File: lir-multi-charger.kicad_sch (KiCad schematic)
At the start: 43 parts, among them J1 USB_C_Receptacle_USB2.0, J2 Conn_01x02_Male, J3 Conn_01x02_Male, J4 Conn_01x02_Male, J5 Conn_01x02_Male, J6 Conn_01x02_Male, U1 CN3130, U2 CN3130, U3 CN3130

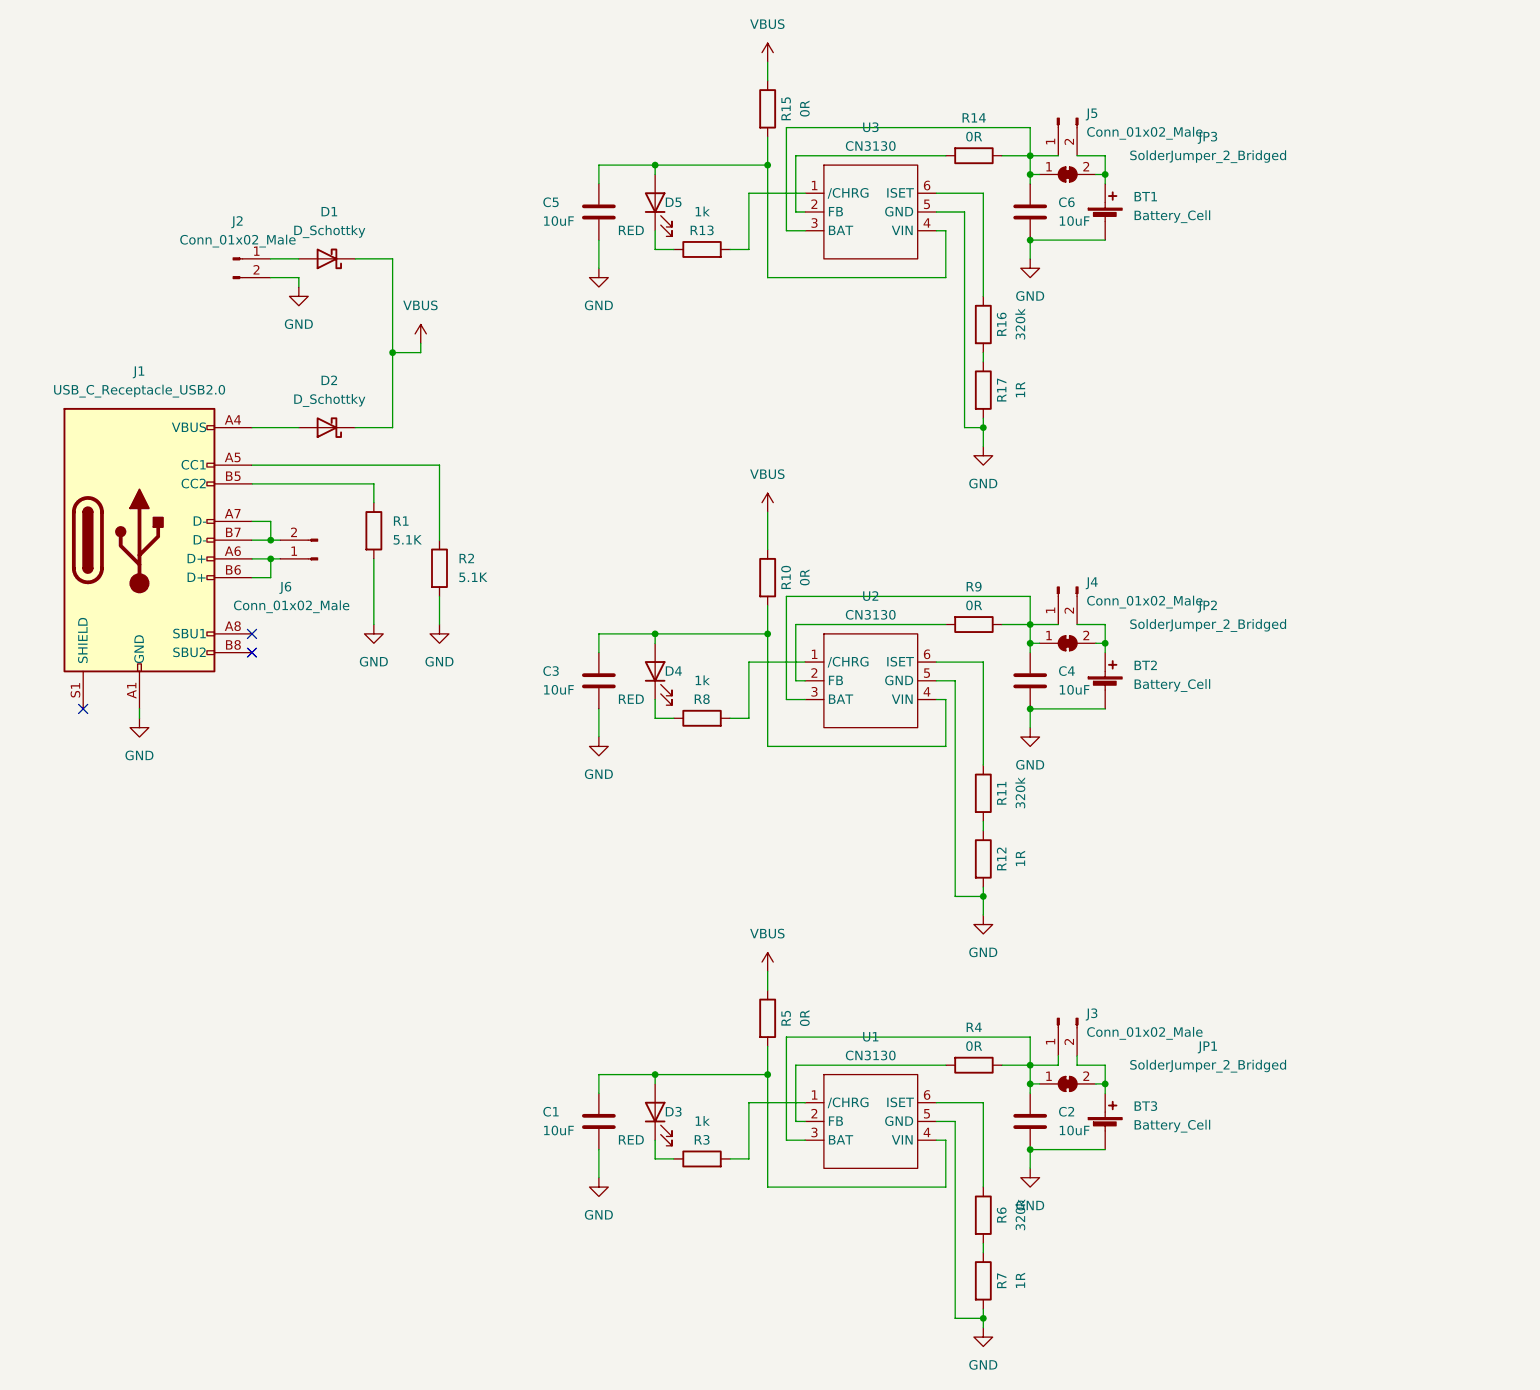
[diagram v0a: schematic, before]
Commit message: Update PCB design for KiCad 7 compatibility and add external battery connector
- Migrated project from KiCad 6 to KiCad 7
- Updated library links and component references for KiCad 7 compatibility
- Added external battery connector terminal block
- Updated project files (.kicad_pro, .kicad_prl, .kicad_sch, .kicad_pcb)
- Updated footprint info cache for new component references
- Added new backup files from recent design iterations
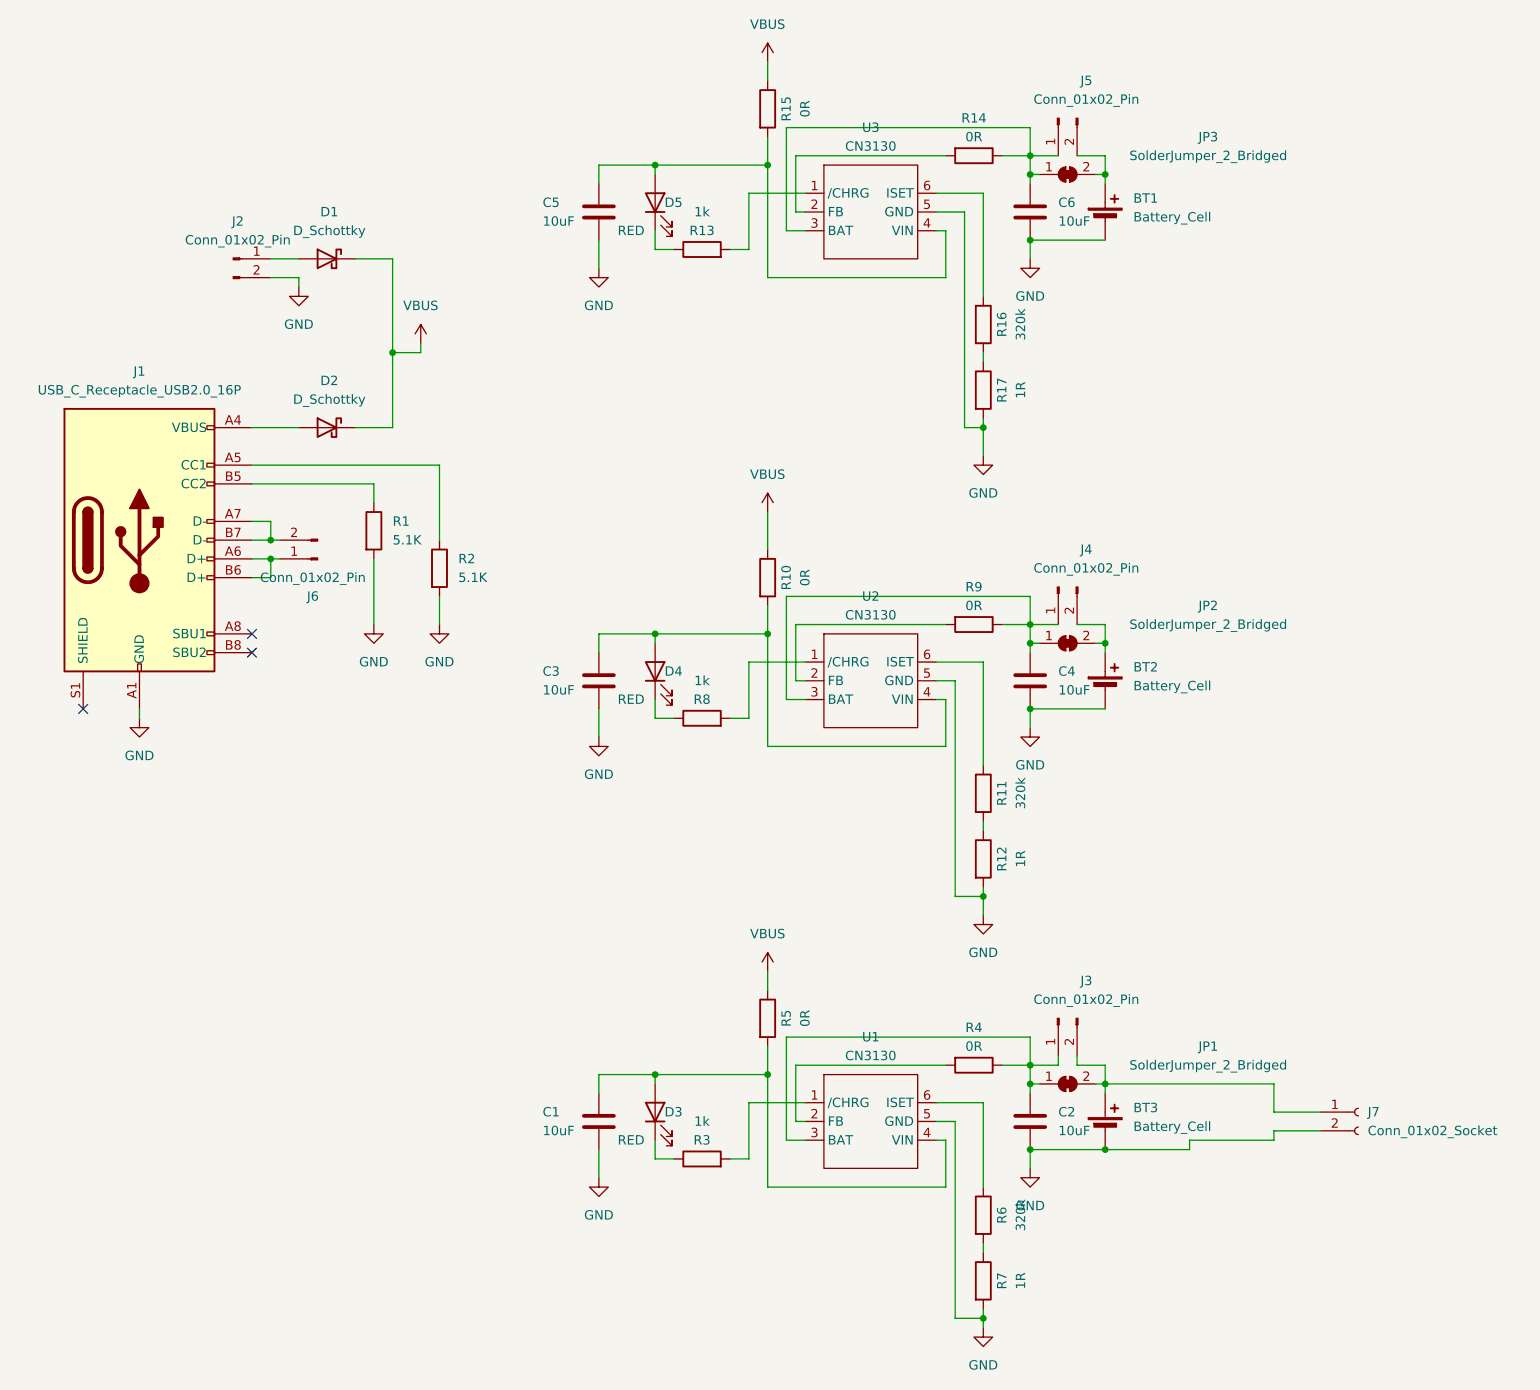
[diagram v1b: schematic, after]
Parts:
- removed J1: USB_C_Receptacle_USB2.0, Connector_USB:USB_C_Receptacle_HRO_TYPE-C-31-M-12, symbol Connector:USB_C_Receptacle_USB2.0
- removed J2, J3, J4, J5, J6: Conn_01x02_Male, Connector_PinHeader_2.54mm:PinHeader_1x02_P2.54mm_Vertical, symbol Connector:Conn_01x02_Male
- added J1: USB_C_Receptacle_USB2.0_16P, Connector_USB:USB_C_Receptacle_HRO_TYPE-C-31-M-12, symbol Connector:USB_C_Receptacle_USB2.0_16P
- added J2, J3, J4, J5, J6: Conn_01x02_Pin, Connector_PinHeader_2.54mm:PinHeader_1x02_P2.54mm_Vertical, symbol Connector:Conn_01x02_Pin
- added J7: Conn_01x02_Socket, TerminalBlock_4Ucon:TerminalBlock_4Ucon_1x02_P3.50mm_Horizontal, symbol Connector:Conn_01x02_Socket
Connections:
- net GND: now also J1.A1 (GND), J1.A12 (GND), J1.B1 (GND), J1.B12 (GND), J2.2 (Pin_2), J7.2 (Pin_2)
- net at D1.2 (A): now also J2.1 (Pin_1)
- net at C4.1, JP2.1 (A), R9.1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: now also J4.1 (Pin_1)
- net at C6.1, JP3.1 (A), R14.1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: now also J5.1 (Pin_1)
- net at R2.1: now also J1.A5 (CC1)
- net at C2.1, JP1.1 (A), R4.1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: now also J3.1 (Pin_1)
- net at BT1.1 (+), JP3.2 (B): now also J5.2 (Pin_2)
- net at D2.2 (A): now also J1.A4 (VBUS), J1.A9 (VBUS), J1.B4 (VBUS), J1.B9 (VBUS)
- net at R1.1: now also J1.B5 (CC2)
- net at BT2.1 (+), JP2.2 (B): now also J4.2 (Pin_2)
- net at BT3.1 (+), JP1.2 (B): now also J3.2 (Pin_2), J7.1 (Pin_1)
- new net: J1.A6 (D+), J1.B6 (D+), J6.1 (Pin_1)
- new net: J1.A7 (D-), J1.B7 (D-), J6.2 (Pin_2)

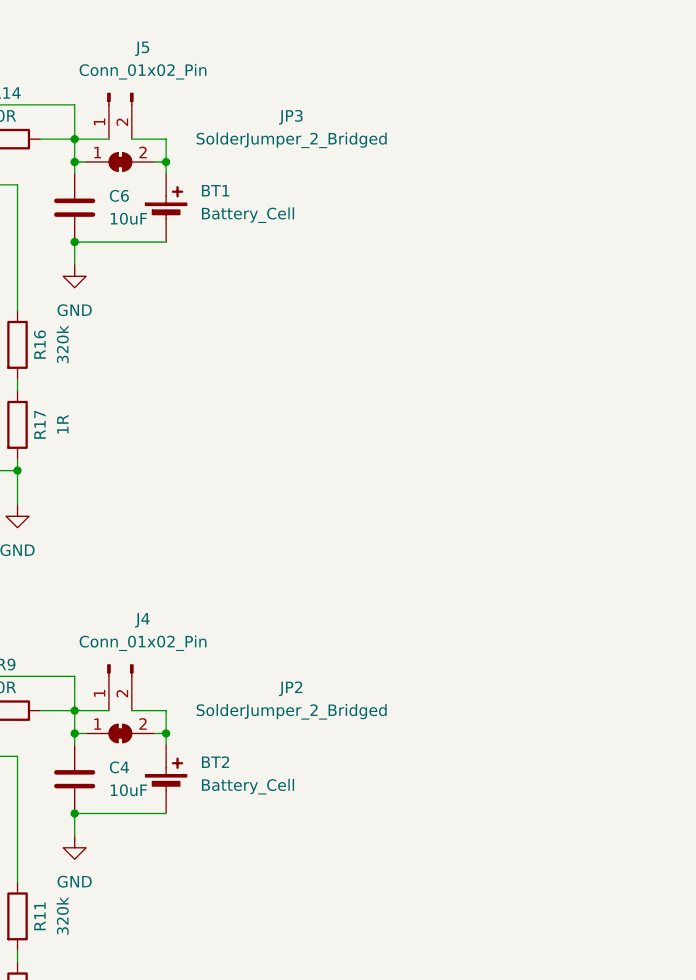
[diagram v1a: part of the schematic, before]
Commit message: Add two screw terminal blocks for external battery connections
- Added TB1 and TB2 terminal blocks to schematic for external battery charging
- Routed PCB layout with new terminal block components
- Connected terminals to power rails for battery input
- Enables external battery charging capability
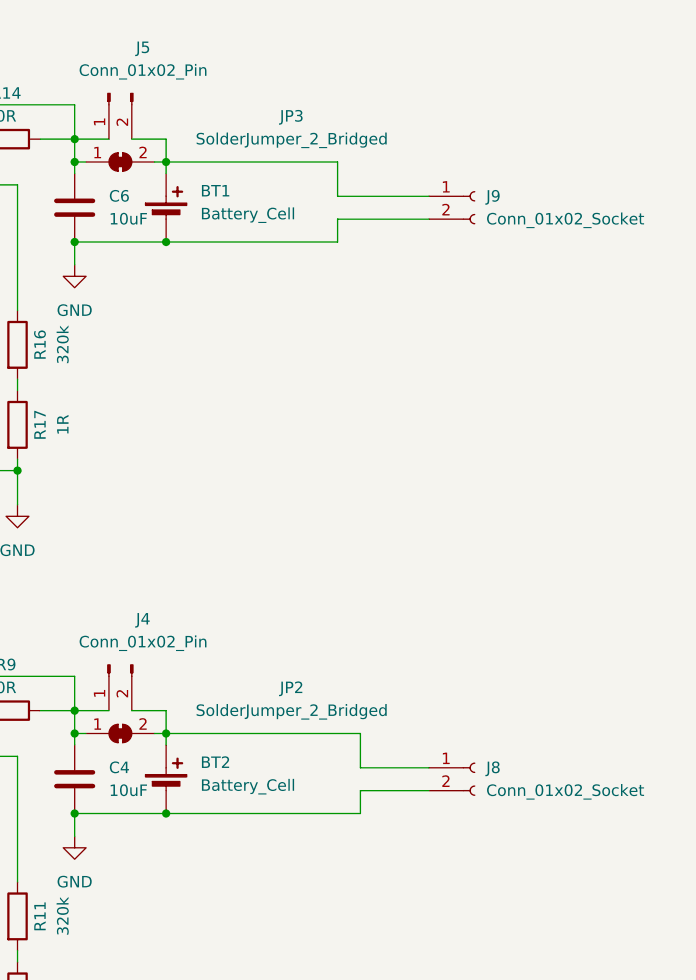
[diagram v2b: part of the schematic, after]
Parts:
- added J8, J9: Conn_01x02_Socket, TerminalBlock_4Ucon:TerminalBlock_4Ucon_1x02_P3.50mm_Horizontal, symbol Connector:Conn_01x02_Socket
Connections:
- net GND: now also J8.2 (Pin_2), J9.2 (Pin_2)
- net at BT1.1 (+), J5.2 (Pin_2), JP3.2 (B): now also J9.1 (Pin_1)
- net at BT2.1 (+), J4.2 (Pin_2), JP2.2 (B): now also J8.1 (Pin_1)
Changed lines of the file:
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@@
   (junction (at 147.32 68.58) (diameter 0) (color 0 0 0 0)
   )
+  (junction (at 163.83 43.18) (diameter 0) (color 0 0 0 0)
+  )
   (junction (at 102.87 96.52) (diameter 0) (color 0 0 0 0)
   )
   (junction (at 153.67 43.18) (diameter 0) (color 0 0 0 0)
+  )
+  (junction (at 163.83 106.68) (diameter 0) (color 0 0 0 0)
   )
   (junction (at 67.31 58.42) (diameter 0) (color 0 0 0 0)
@@
     (stroke (width 0) (type default))
   )
+  (wire (pts (xy 182.88 34.29) (xy 182.88 38.1))
+    (stroke (width 0) (type default))
+  )
   (wire (pts (xy 160.02 154.94) (xy 163.83 154.94))
     (stroke (width 0) (type default))
@@
     (stroke (width 0) (type default))
   )
+  (wire (pts (xy 185.42 104.14) (xy 193.04 104.14))
+    (stroke (width 0) (type default))
+  )
+  (wire (pts (xy 185.42 97.79) (xy 185.42 101.6))
+    (stroke (width 0) (type default))
+  )
   (wire (pts (xy 140.97 165.1) (xy 142.24 165.1))
     (stroke (width 0) (type default))
@@
     (stroke (width 0) (type default))
   )
+  (wire (pts (xy 163.83 97.79) (xy 185.42 97.79))
+    (stroke (width 0) (type default))
+  )
   (wire (pts (xy 163.83 157.48) (xy 186.69 157.48))
     (stroke (width 0) (type default))
@@
     (stroke (width 0) (type default))
   )
+  (wire (pts (xy 163.83 106.68) (xy 185.42 106.68))
+    (stroke (width 0) (type default))
+  )
   (wire (pts (xy 162.56 34.29) (xy 163.83 34.29))
     (stroke (width 0) (type default))
@@
     (stroke (width 0) (type default))
   )
+  (wire (pts (xy 182.88 43.18) (xy 182.88 40.64))
+    (stroke (width 0) (type default))
+  )
   (wire (pts (xy 157.48 95.25) (xy 153.67 95.25))
     (stroke (width 0) (type default))
@@
     (stroke (width 0) (type default))
   )
+  (wire (pts (xy 163.83 34.29) (xy 182.88 34.29))
+    (stroke (width 0) (type default))
+  )
   (wire (pts (xy 118.11 19.05) (xy 118.11 21.59))
     (stroke (width 0) (type default))
@@
     (stroke (width 0) (type default))
   )
+  (wire (pts (xy 163.83 43.18) (xy 182.88 43.18))
+    (stroke (width 0) (type default))
+  )
   (wire (pts (xy 147.32 189.23) (xy 147.32 190.5))
     (stroke (width 0) (type default))
@@
     (stroke (width 0) (type default))
   )
+  (wire (pts (xy 185.42 106.68) (xy 185.42 104.14))
+    (stroke (width 0) (type default))
+  )
   (wire (pts (xy 64.77 86.36) (xy 64.77 95.25))
     (stroke (width 0) (type default))
@@
     (stroke (width 0) (type default))
   )
+  (wire (pts (xy 185.42 101.6) (xy 193.04 101.6))
+    (stroke (width 0) (type default))
+  )
   (wire (pts (xy 123.19 160.02) (xy 115.57 160.02))
     (stroke (width 0) (type default))
@@
     (stroke (width 0) (type default))
   )
+  (wire (pts (xy 182.88 40.64) (xy 193.04 40.64))
+    (stroke (width 0) (type default))
+  )
   (wire (pts (xy 120.65 151.13) (xy 153.67 151.13))
     (stroke (width 0) (type default))
@@
   )
   (wire (pts (xy 157.48 31.75) (xy 153.67 31.75))
+    (stroke (width 0) (type default))
+  )
+  (wire (pts (xy 182.88 38.1) (xy 193.04 38.1))
     (stroke (width 0) (type default))
   )
@@
         (path "/14b6b0e6-9069-4fd8-8488-b92cc2dc5275"
           (reference "#PWR0108") (unit 1)
+        )
+      )
+    )
+  )
+  (symbol (lib_id "Connector:Conn_01x02_Socket") (at 198.12 101.6 0) (unit 1)
+    (in_bom yes) (on_board yes) (dnp no) (fields_autoplaced)
+    (property "Reference" "J8" (at 199.39 101.6 0)
+      (effects (font (size 1.27 1.27)) (justify left))
+    )
+    (property "Value" "Conn_01x02_Socket" (at 199.39 104.14 0)
+      (effects (font (size 1.27 1.27)) (justify left))
+    )
+    (property "Footprint" "TerminalBlock_4Ucon:TerminalBlock_4Ucon_1x02_P3.50mm_Horizontal" (at 198.12 101.6 0)
+      (effects (font (size 1.27 1.27)) hide)
+    )
+    (property "Datasheet" "~" (at 198.12 101.6 0)
+      (effects (font (size 1.27 1.27)) hide)
+    )
+    (pin "2")
+    (pin "1")
+    (instances
+      (project "lir-multi-charger"
+        (path "/14b6b0e6-9069-4fd8-8488-b92cc2dc5275"
+          (reference "J8") (unit 1)
         )
       )
@@
         )
       )
+    )
+  )
+  (symbol (lib_id "Connector:Conn_01x02_Socket") (at 198.12 38.1 0) (unit 1)
+    (in_bom yes) (on_board yes) (dnp no) (fields_autoplaced)
+    (property "Reference" "J9" (at 199.39 38.1 0)
+      (effects (font (size 1.27 1.27)) (justify left))
+    )
+    (property "Value" "Conn_01x02_Socket" (at 199.39 40.64 0)
+      (effects (font (size 1.27 1.27)) (justify left))
+    )
+    (property "Footprint" "TerminalBlock_4Ucon:TerminalBlock_4Ucon_1x02_P3.50mm_Horizontal" (at 198.12 38.1 0)
+      (effects (font (size 1.27 1.27)) hide)
+    )
+    (property "Datasheet" "~" (at 198.12 38.1 0)
+      (effects (font (size 1.27 1.27)) hide)
+    )
+    (pin "2")
+    (pin "1")
+    (instances
+      (project "lir-multi-charger"
+        (path "/14b6b0e6-9069-4fd8-8488-b92cc2dc5275"
+          (reference "J9") (unit 1)
+        )
+      )
